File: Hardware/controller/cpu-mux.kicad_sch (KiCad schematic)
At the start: 7 parts

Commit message: Replaced most passives with 0603 size
- This is more compact, and we might as well since this board will be at
  least partially assembled beforehand
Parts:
- C, U: MPN CL21B104KACNFNC -> (none)
- U: MPN RMC1/10-222JTP -> (none)
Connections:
- no-connect marks 0 -> 3
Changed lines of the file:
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@@
   (junction (at 133.985 74.93) (diameter 0) (color 0 0 0 0)
   )
+  (no_connect (at 155.575 45.72))
+  (no_connect (at 137.795 45.72))
+  (no_connect (at 155.575 48.26))
   (wire (pts (xy 131.445 100.33) (xy 132.715 100.33))
     (stroke (width 0) (type default))
@@
       (effects (font (size 1.27 1.27)) hide)
     )
-    (property "MPN" "CL21B104KACNFNC" (id 4) (at 133.985 72.39 0)
+    (property "MPN" "" (id 4) (at 133.985 72.39 0)
       (effects (font (size 1.27 1.27)) hide)
     )
@@
       (effects (font (size 1.27 1.27)) hide)
     )
-    (property "MPN" "RMC1/10-222JTP" (id 4) (at 50.165 83.82 90)
+    (property "MPN" "" (id 4) (at 50.165 83.82 90)
       (effects (font (size 1.27 1.27)) hide)
     )
@@
       (effects (font (size 1.27 1.27)) hide)
     )
-    (property "MPN" "CL21B104KACNFNC" (id 4) (at 73.025 60.325 0)
+    (property "MPN" "" (id 4) (at 73.025 60.325 0)
       (effects (font (size 1.27 1.27)) hide)
     )
@@
       (effects (font (size 1.27 1.27)) hide)
     )
-    (property "MPN" "RMC1/10-222JTP" (id 4) (at 50.165 75.565 90)
-      (effects (font (size 1.27 1.27)) hide)
-    )
+    (property "MPN" "" (id 4) (at 50.165 75.565 90)
+      (effects (font (size 1.27 1.27)) hide)
+    )

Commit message: Auxiliary I2C + SPI bus routing
- Added an I2C MAC EEPROM to the aux I2C bus, which will be read for the
  device serial and Ethernet MAC address

- Add fan controller, filtering/ESD and fusing for expansion connector
  for rear IO section. We'll still have to add the CAN termination as
  well as the CAN transceiver on that part

- Minor routing + pin location tweaks
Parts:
- added U (x2): (no value), symbol Device:R_Small
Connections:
- net +3V3: now also U.2, U.2
- net IO_I2C_SCL: now also U.1
- net IO_I2C_SDA: now also U.1
- net IO_SPI_SCK: now reaches U.11 (3B1)
- net IO_SPI_MISO: now reaches U.14 (4B1)
- net IO_SPI_MOSI: now reaches U.2 (1B1)
- net ~{SPI_CS0} renamed ~{IO_SPI_CS}
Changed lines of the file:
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@@
   (junction (at 73.025 57.785) (diameter 0) (color 0 0 0 0)
   )
+  (junction (at 44.45 92.075) (diameter 0) (color 0 0 0 0)
+  )
   (junction (at 44.45 75.565) (diameter 0) (color 0 0 0 0)
+  )
+  (junction (at 44.45 83.82) (diameter 0) (color 0 0 0 0)
   )
   (junction (at 133.985 74.93) (diameter 0) (color 0 0 0 0)
@@
     (stroke (width 0) (type default))
   )
+  (wire (pts (xy 44.45 92.075) (xy 47.625 92.075))
+    (stroke (width 0) (type default))
+  )
   (wire (pts (xy 155.575 52.07) (xy 156.845 52.07))
     (stroke (width 0) (type default))
@@
     (stroke (width 0) (type default))
   )
+  (wire (pts (xy 52.705 100.33) (xy 65.405 100.33))
+    (stroke (width 0) (type default))
+  )
   (wire (pts (xy 67.31 60.325) (xy 69.85 60.325))
     (stroke (width 0) (type default))
@@
     (stroke (width 0) (type default))
   )
+  (wire (pts (xy 52.705 92.075) (xy 65.405 92.075))
+    (stroke (width 0) (type default))
+  )
+  (wire (pts (xy 44.45 92.075) (xy 44.45 83.82))
+    (stroke (width 0) (type default))
+  )
   (wire (pts (xy 136.525 63.5) (xy 137.795 63.5))
     (stroke (width 0) (type default))
@@
     (stroke (width 0) (type default))
   )
+  (wire (pts (xy 44.45 100.33) (xy 47.625 100.33))
+    (stroke (width 0) (type default))
+  )
   (wire (pts (xy 44.45 83.82) (xy 47.625 83.82))
     (stroke (width 0) (type default))
@@
   )
   (wire (pts (xy 186.69 41.91) (xy 187.96 41.91))
+    (stroke (width 0) (type default))
+  )
+  (wire (pts (xy 44.45 100.33) (xy 44.45 92.075))
     (stroke (width 0) (type default))
   )
@@
     (effects (font (size 1.27 1.27)) (justify right bottom))
   )
+  (label "IO_I2C_SDA" (at 65.405 100.33 0) (fields_autoplaced)
+    (effects (font (size 1.27 1.27)) (justify right bottom))
+  )
+  (label "IO_I2C_SCL" (at 65.405 92.075 0) (fields_autoplaced)
+    (effects (font (size 1.27 1.27)) (justify right bottom))
+  )
   (label "~{SPI_MUX_OE}" (at 165.1 100.33 0) (fields_autoplaced)
     (effects (font (size 1.27 1.27)) (justify right bottom))
@@
     (effects (font (size 1.27 1.27)) (justify left))
   )
+  (hierarchical_label "IO_SPI_MOSI" (shape output) (at 156.845 39.37 0) (fields_autoplaced)
+    (effects (font (size 1.27 1.27)) (justify left))
+  )
+  (hierarchical_label "~{IO_SPI_CS}" (shape output) (at 187.96 41.91 0) (fields_autoplaced)
+    (effects (font (size 1.27 1.27)) (justify left))
+  )
   (hierarchical_label "DISP_SPI_SCK" (shape output) (at 156.845 54.61 0) (fields_autoplaced)
     (effects (font (size 1.27 1.27)) (justify left))
@@
     (effects (font (size 1.27 1.27)) (justify right))
   )
+  (hierarchical_label "IO_SPI_MISO" (shape input) (at 156.845 58.42 0) (fields_autoplaced)
+    (effects (font (size 1.27 1.27)) (justify left))
+  )
   (hierarchical_label "FRONT_I2C_SDA" (shape bidirectional) (at 40.64 40.005 180) (fields_autoplaced)
     (effects (font (size 1.27 1.27)) (justify right))
@@
   (hierarchical_label "SPI_SCK" (shape input) (at 136.525 52.07 180) (fields_autoplaced)
     (effects (font (size 1.27 1.27)) (justify right))
+  )
+  (hierarchical_label "IO_SPI_SCK" (shape output) (at 156.845 52.07 0) (fields_autoplaced)
+    (effects (font (size 1.27 1.27)) (justify left))
   )
   (hierarchical_label "~{IO_I2C_IRQ}" (shape input) (at 40.64 45.085 180) (fields_autoplaced)
@@
     )
     (pin "1")
+  )
+  (symbol (lib_id "Device:R_Small") (at 50.165 92.075 270) (mirror x) (unit 1)
+    (in_bom yes) (on_board yes)
+    (default_instance (reference "U") (unit 1) (value "") (footprint ""))
+    (property "Reference" "U" (id 0) (at 50.165 86.995 90)
+      (effects (font (size 1.27 1.27)))
+    )
+    (property "Value" "" (id 1) (at 50.165 89.535 90)
+      (effects (font (size 1.27 1.27)))
+    )
+    (property "Footprint" "" (id 2) (at 50.165 92.075 0)
+      (effects (font (size 1.27 1.27)) hide)
+    )
+    (property "Datasheet" "~" (id 3) (at 50.165 92.075 0)
+      (effects (font (size 1.27 1.27)) hide)
+    )
+    (property "MPN" "" (id 4) (at 50.165 92.075 90)
+      (effects (font (size 1.27 1.27)) hide)
+    )
+    (pin "1")
+    (pin "2")
   )
   (symbol (lib_id "power:+3V3") (at 44.45 75.565 0) (unit 1)
@@
     (pin "1")
   )
+  (symbol (lib_id "Device:R_Small") (at 50.165 100.33 270) (mirror x) (unit 1)
+    (in_bom yes) (on_board yes)
+    (default_instance (reference "U") (unit 1) (value "") (footprint ""))
+    (property "Reference" "U" (id 0) (at 50.165 95.25 90)
+      (effects (font (size 1.27 1.27)))
+    )
+    (property "Value" "" (id 1) (at 50.165 97.79 90)
+      (effects (font (size 1.27 1.27)))
+    )
+    (property "Footprint" "" (id 2) (at 50.165 100.33 0)
+      (effects (font (size 1.27 1.27)) hide)
+    )
+    (property "Datasheet" "~" (id 3) (at 50.165 100.33 0)
+      (effects (font (size 1.27 1.27)) hide)
+    )
+    (property "MPN" "" (id 4) (at 50.165 100.33 90)
+      (effects (font (size 1.27 1.27)) hide)
+    )
+    (pin "1")
+    (pin "2")
+  )
   (symbol (lib_id "power:GND") (at 73.025 62.865 0) (unit 1)

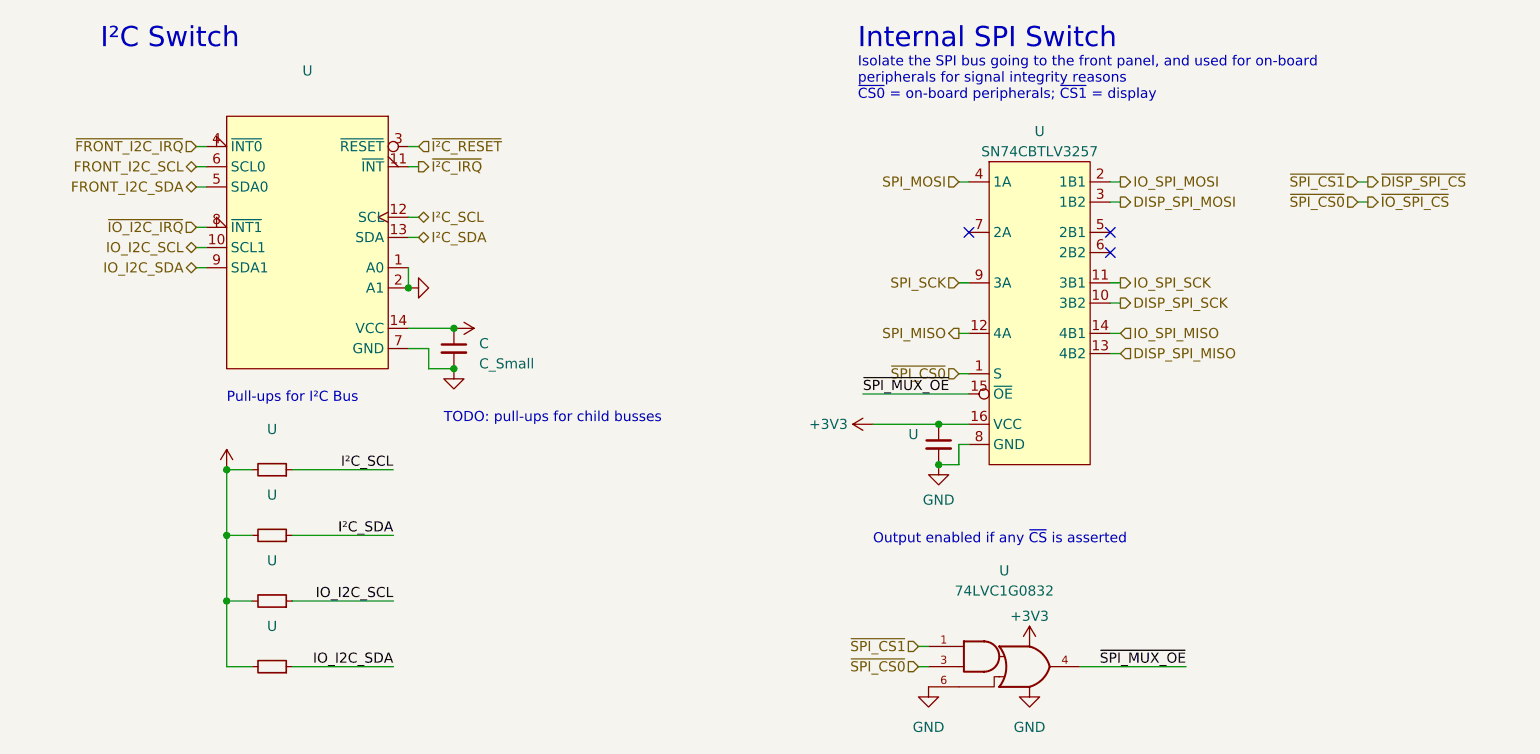
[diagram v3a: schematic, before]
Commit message: hw: start working on rev4 controller
- removed SPI for display, and the associated SPI mux nonsense, and any
  superfluous resistors for pull-ups

- removed MAC address EEPROM

- start adding i2c RTC (which will also contain EEPROM with the MAC of
  the system, lol)

- start moving some components from bottom to top side of board

- tweaked positions of some mains voltage traces

- increased values of power indicator LED's current dropping resistors

- take 3V3 from SoM rather than generate it ourselves
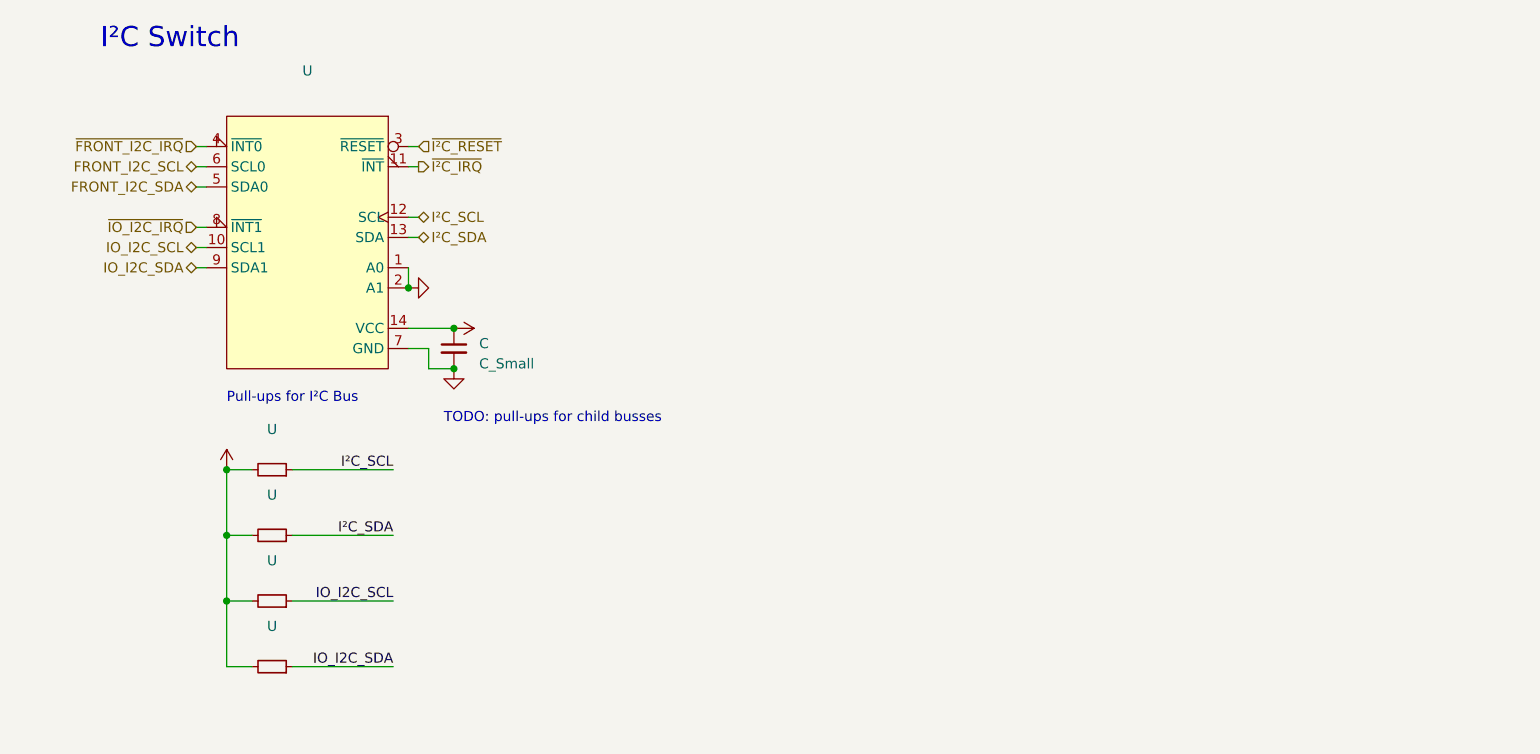
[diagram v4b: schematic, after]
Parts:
- removed U: (no value), symbol Device:C_Small
- removed U: 74LVC1G0832, symbol 74xGxx:74LVC1G0832
- removed U: SN74CBTLV3257, symbol programmable-load:SN74CBTLV3257
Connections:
- no-connect marks 3 -> 0
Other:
- note removed: "Internal SPI Switch"
- note removed: "Isolate the SPI bus going to the front panel, and used for on-board peripherals for signal integrity reasons ~{CS0} = on-board peripherals; ~{CS1} = display"
- note removed: "Output enabled if any ~{CS} is asserted"
- title: (none) -> Programmable Load Controller

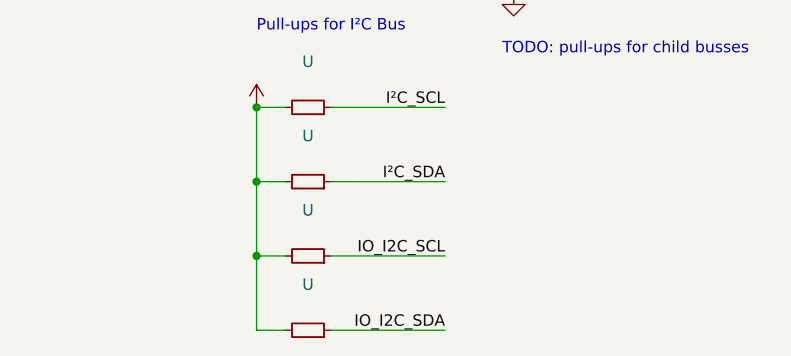
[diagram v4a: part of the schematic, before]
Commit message: hw: start reworking power section
- replace the integrated power modules with a discrete power supply
  based around TPS54331 chip; so far this has been replaced for the +12V
  supply (complete with layout)

- added footprints for a few different inductors

- create footprint for TPS54331 DC/DC converter
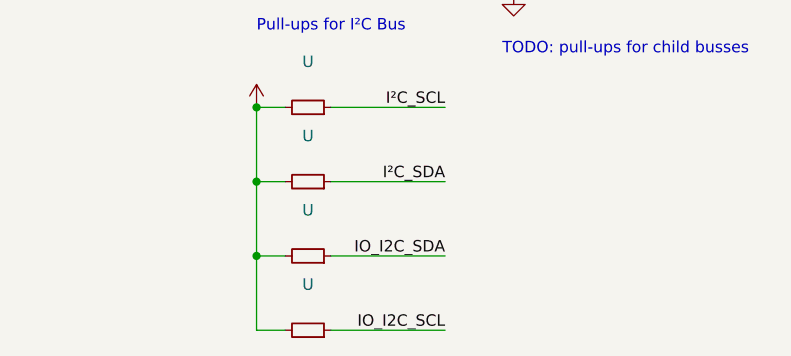
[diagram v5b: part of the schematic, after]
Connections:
- net IO_I2C_SCL: now also U.1; no longer U.1
- net IO_I2C_SDA: now also U.1; no longer U.1
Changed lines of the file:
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@@
     (effects (font (size 1.27 1.27)) (justify right bottom))
   )
-  (label "IO_I2C_SDA" (at 65.405 100.33 0) (fields_autoplaced)
+  (label "IO_I2C_SCL" (at 65.405 100.33 0) (fields_autoplaced)
     (effects (font (size 1.27 1.27)) (justify right bottom))
   )
-  (label "IO_I2C_SCL" (at 65.405 92.075 0) (fields_autoplaced)
+  (label "IO_I2C_SDA" (at 65.405 92.075 0) (fields_autoplaced)
     (effects (font (size 1.27 1.27)) (justify right bottom))
   )

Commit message: hw: add charger for RTC
- added RTC supercapacitor

- added the charging circuit for the RTC (with adjustment for voltage
  and all that fun stuff) based around a bonus linear regulator for the
  supercap

- minor tweaks all around: add more JLCPCB part numbers and fixed some
  footprints for some components
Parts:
- U: JLCPCB (none) -> C4190
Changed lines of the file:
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@@
+      (effects (font (size 1.27 1.27)) hide)
+    )
+    (property "JLCPCB" "C4190" (id 5) (at 50.165 92.075 90)
       (effects (font (size 1.27 1.27)) hide)
     )
@@
       (effects (font (size 1.27 1.27)) hide)
     )
+    (property "JLCPCB" "C4190" (id 5) (at 50.165 83.82 90)
+      (effects (font (size 1.27 1.27)) hide)
+    )
     (pin "1")
     (pin "2")
@@
     )
     (property "MPN" "" (id 4) (at 50.165 100.33 90)
+      (effects (font (size 1.27 1.27)) hide)
+    )
+    (property "JLCPCB" "C4190" (id 5) (at 50.165 100.33 90)
       (effects (font (size 1.27 1.27)) hide)
     )
@@
       (effects (font (size 1.27 1.27)) hide)
     )
+    (property "JLCPCB" "C4190" (id 5) (at 50.165 75.565 90)
+      (effects (font (size 1.27 1.27)) hide)
+    )

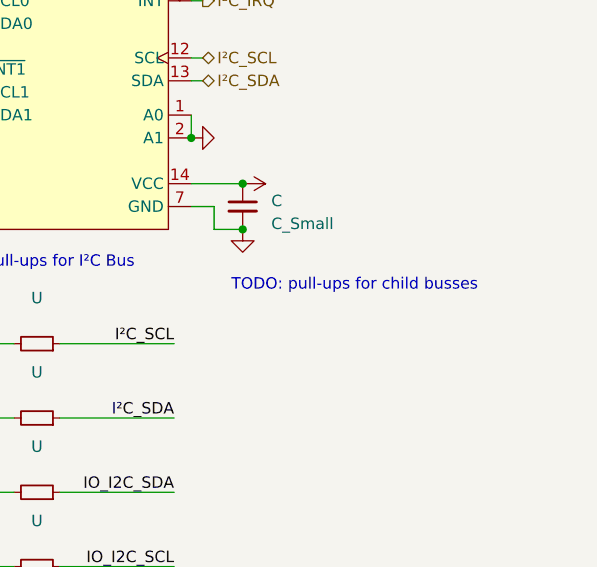
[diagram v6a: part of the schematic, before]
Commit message: hw: add more part numbers, cleanup
- Added JLCPCB part numbers for more passive components

- Added a status LED for the rear of the board (next to the device USB
  port)
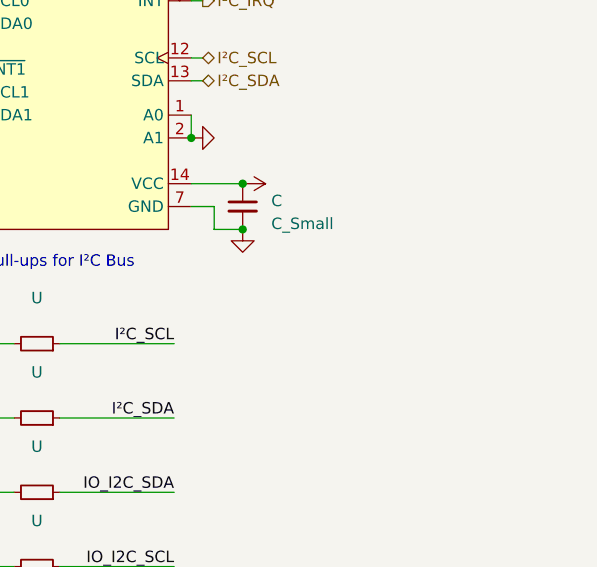
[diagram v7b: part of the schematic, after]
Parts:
- C: JLCPCB (none) -> C14663
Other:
- note removed: "TODO: pull-ups for child busses"
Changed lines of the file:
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@@
     (stroke (width 0) (type default))
-  )
-  (text "TODO: pull-ups for child busses" (at 71.755 69.85 0)
-    (effects (font (size 1.27 1.27)) (justify left bottom))
   )
   (text "Pull-ups for I²C Bus\n" (at 44.45 67.31 0)
@@
       (effects (font (size 1.27 1.27)) hide)
     )
+    (property "JLCPCB" "C14663" (id 5) (at 73.025 60.325 0)
+      (effects (font (size 1.27 1.27)) hide)
+    )
